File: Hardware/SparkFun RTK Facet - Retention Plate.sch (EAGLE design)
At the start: 31 parts, among them J1 FPC_12_0.5MM2, J16 microSD, J17 NANO_SIM, J2 FPC_12_0.5MM2, U13 LIS2DH12

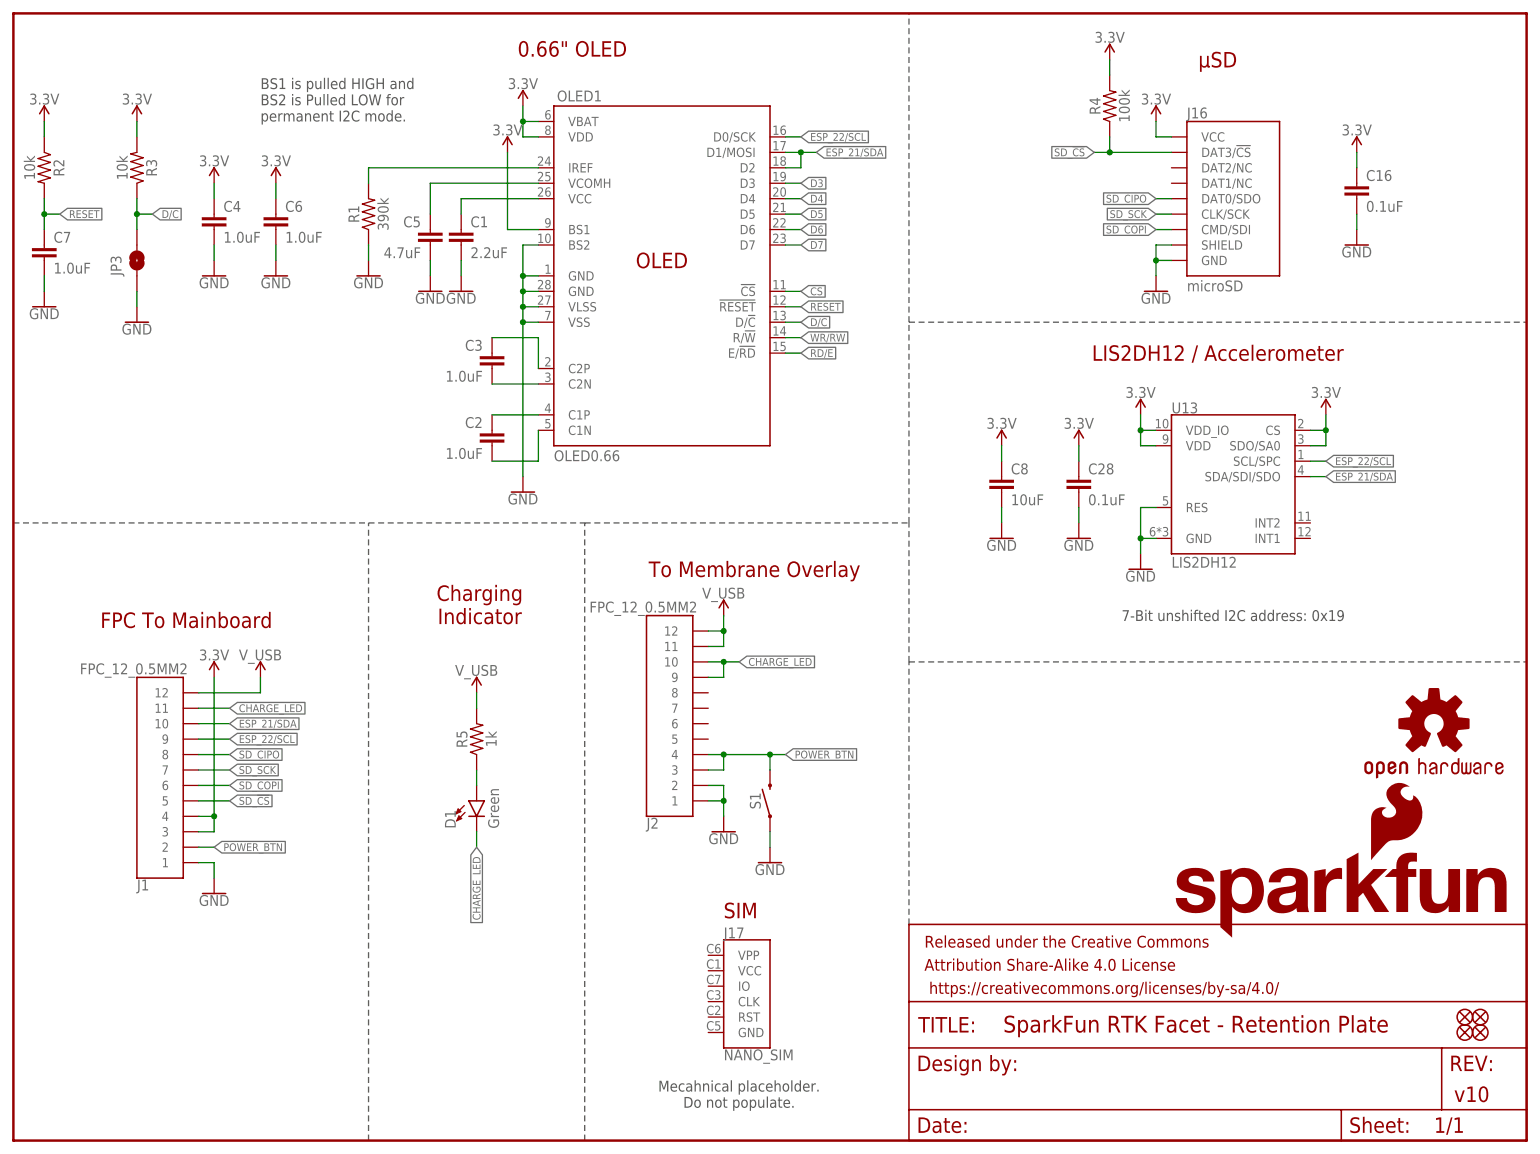
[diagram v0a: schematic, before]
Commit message: Move display connector to side so overlay connector can be center. Notch PCBs. Add dummy PCB height. Add dummy retention plate.
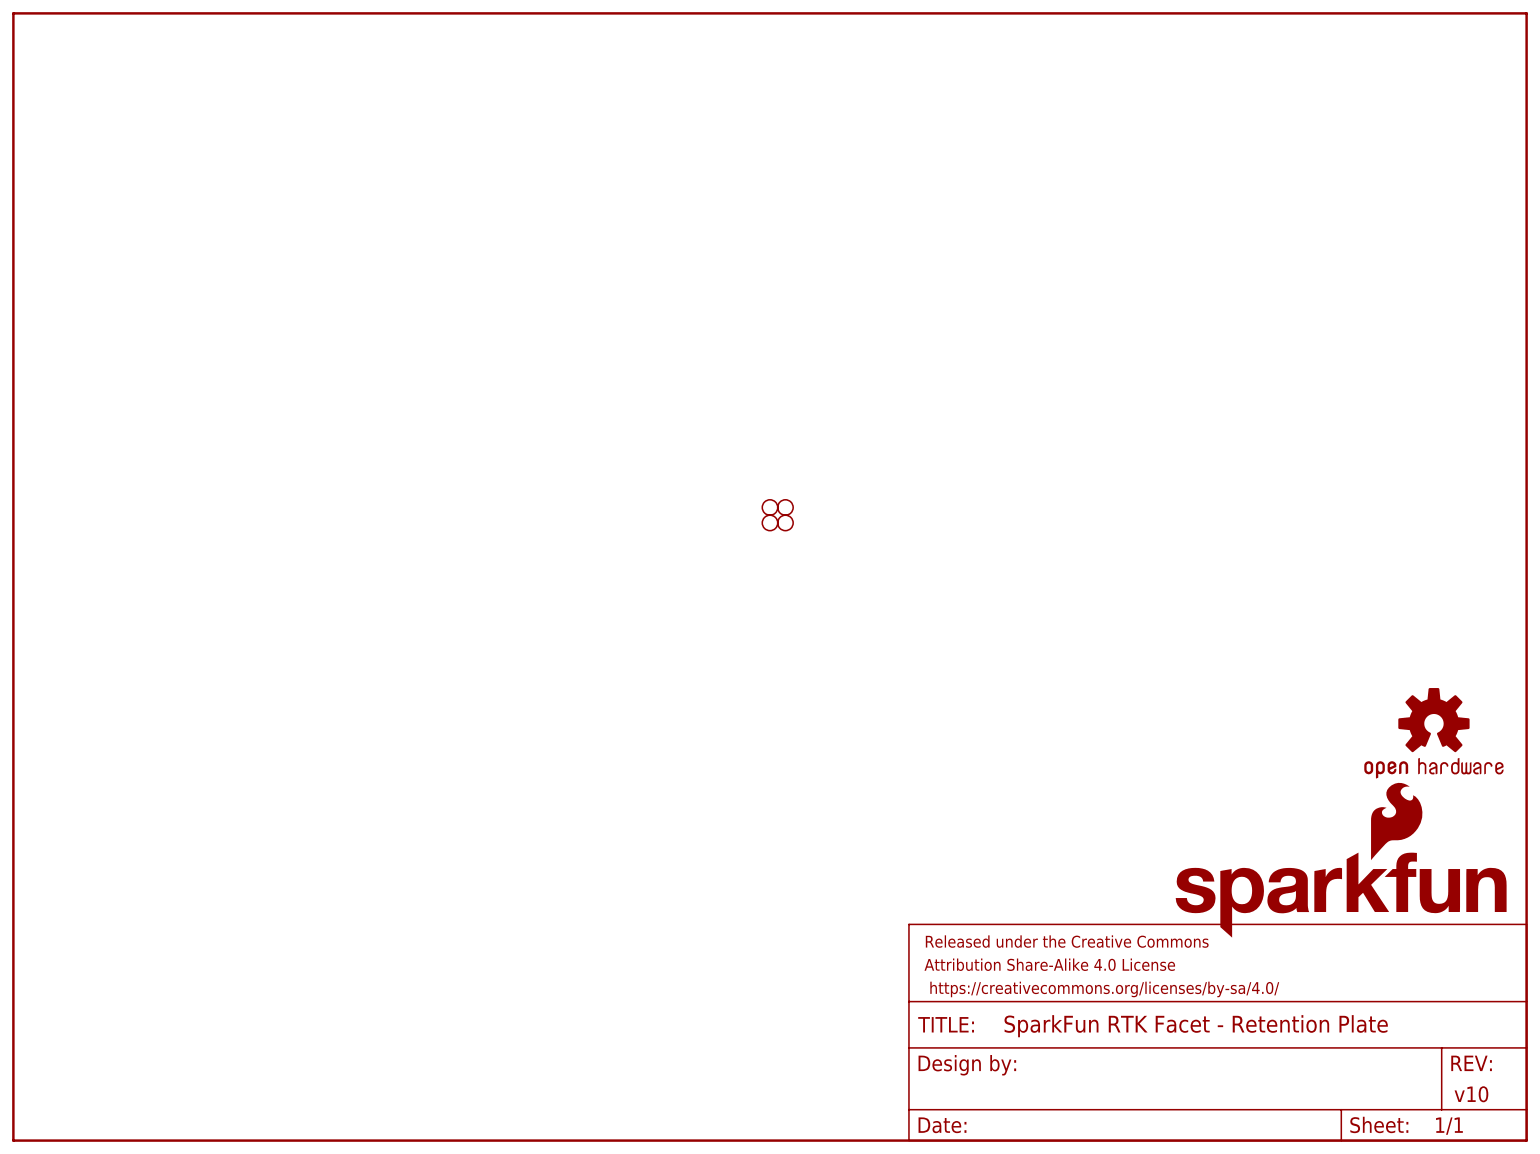
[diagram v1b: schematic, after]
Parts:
- removed C1: 2.2uF, SparkFun-Capacitors:2.2UF-0805-25V-(+80/-20%)
- removed C16, C28: 0.1uF, SparkFun-Capacitors:0.1UF-0603-25V-(+80/-20%)
- removed C2, C3: 1.0uF, SparkFun-Capacitors:1.0UF-0805-25V-10%
- removed C4, C6, C7: 1.0uF, SparkFun-Capacitors:1.0UF-0603-16V-10%
- removed C5: 4.7uF, SparkFun-Capacitors:4.7UF-1206-16V-(+80/-20%)
- removed C8: 10uF, SparkFun-Capacitors:10UF-0603-6.3V-20%
- removed D1: Green, SparkFun-LED:LED-GREEN1206-BOTTOM
- removed FID1, FID2, FID3, FID4: FIDUCIAL1X2, SparkFun-Aesthetics:FIDUCIAL1X2
- removed J1, J2: FPC_12_0.5MM2, RTK Facet:FPC_12_0.5MM2
- removed J16: microSD, SparkFun-Connectors:MICRO-SD-SDIOPUSH-PUSH
- removed J17: NANO_SIM, ublox:NANO_SIMWURTH
- removed JP3: JUMPER-SMT_2_NO_SILK, SparkFun-Jumpers:JUMPER-SMT_2_NO_SILK
- removed OLED1: OLED0.66, SparkFun-Displays:OLED0.66
- removed R1: 390k, SparkFun-Resistors:390KOHM-0603-1/10W-1%
- removed R2, R3: 10k, SparkFun-Resistors:10KOHM-0603-1/10W-1%
- removed R4: 100k, SparkFun-Resistors:100KOHM-0603-1/10W-1%
- removed R5: 1k, SparkFun-Resistors:1KOHM-0603-1/10W-1%
- removed S1: MOMENTARY-SWITCH-SPST-SMD-5.2MM-TALL, SparkFun-Switches:MOMENTARY-SWITCH-SPST-SMD-5.2MM-TALL
- removed U13: LIS2DH12, SparkFun-Sensors:LIS2DH12
- added H1, H2, H3, H4: STAND-OFF, SparkFun-Hardware:STAND-OFF
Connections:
- removed net 3.3V: C16.1, C28.1, C4.1, C6.1, C8.1, J1.3, J1.4, J16.VCC, OLED1.BS1, OLED1.VBAT, OLED1.VDD, R2.1, R3.2, R4.2, U13.CS, U13.SDO/SA0, U13.VDD, U13.VDD_IO
- removed net C1P: C2.1, OLED1.C1P
- removed net C2N: C3.2, OLED1.C2N
- removed net CHARGE_LED: D1.C, J1.11, J2.10, J2.9
- removed net CS: OLED1.!CS!
- removed net D/C: JP3.2, OLED1.D/!C!, R3.1
- removed net D3: OLED1.D3
- removed net D4: OLED1.D4
- removed net D5: OLED1.D5
- removed net D6: OLED1.D6
- removed net D7: OLED1.D7
- removed net ESP_21/SDA: J1.10, OLED1.D1/MOSI, OLED1.D2, U13.SDA/SDI/SDO
- removed net ESP_22/SCL: J1.9, OLED1.D0/SCK, U13.SCL/SPC
- removed net GND: C1.2, C16.2, C28.2, C4.2, C5.2, C6.2, C7.2, C8.2, J1.1, J16.GND, J16.SHIELD, J2.1, J2.2, JP3.1, OLED1.BS2, OLED1.GND@1, OLED1.GND@2, OLED1.VLSS, OLED1.VSS, R1.1, S1.1, U13.GND, U13.RES
- removed net IREF: OLED1.IREF, R1.2
- removed net N$1: C3.1, OLED1.C2P
- removed net N$2: C2.2, OLED1.C1N
- removed net N$3: D1.A, R5.1
- removed net POWER_BTN: J1.2, J2.3, J2.4, S1.2
- removed net RD/E: OLED1.E/!RD!
- removed net RESET: C7.1, OLED1.!RESET!, R2.2
- removed net SD_!CS!: J1.5, J16.DAT3/!CS!, R4.1
- removed net SD_CIPO: J1.8, J16.DAT0/SDO
- removed net SD_COPI: J1.6, J16.CMD/SDI
- removed net SD_SCK: J1.7, J16.CLK/SCK
- removed net VCC: C1.1, OLED1.VCC
- removed net VCOMH: C5.1, OLED1.VCOMH
- removed net V_USB: J1.12, J2.11, J2.12, R5.2
- removed net WR/RW: OLED1.R/!W!
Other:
- note removed: "0.66" OLED"
- note removed: "7-Bit unshifted I2C address: 0x19"
- note removed: "BS1 is pulled HIGH and BS2 is Pulled LOW for permanent I2C mode."
- note removed: "Charging Indicator"
- note removed: "FPC To Mainboard"
- note removed: "LIS2DH12 / Accelerometer"
- note removed: "Mecahnical placeholder. Do not populate."
- note removed: "SIM"
- note removed: "To Membrane Overlay"
- note removed: "μSD"

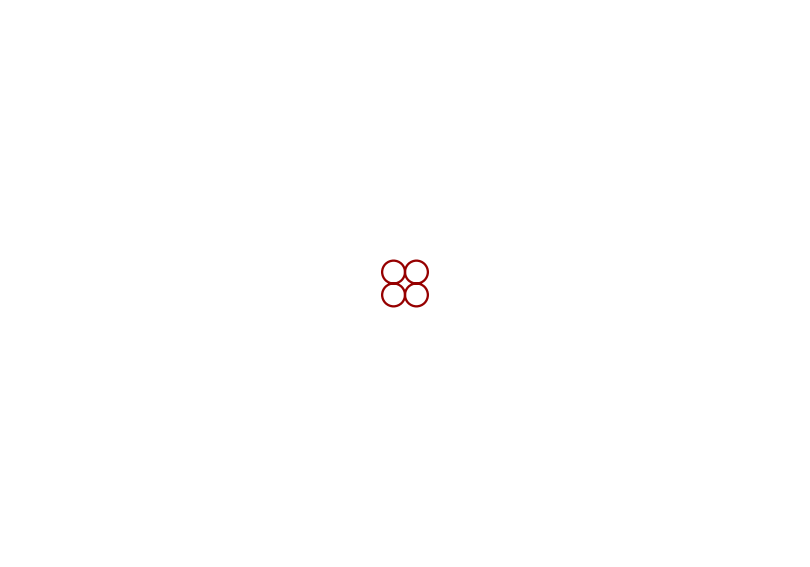
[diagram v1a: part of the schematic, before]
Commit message: Update Retention Plate design as per current Fusion model
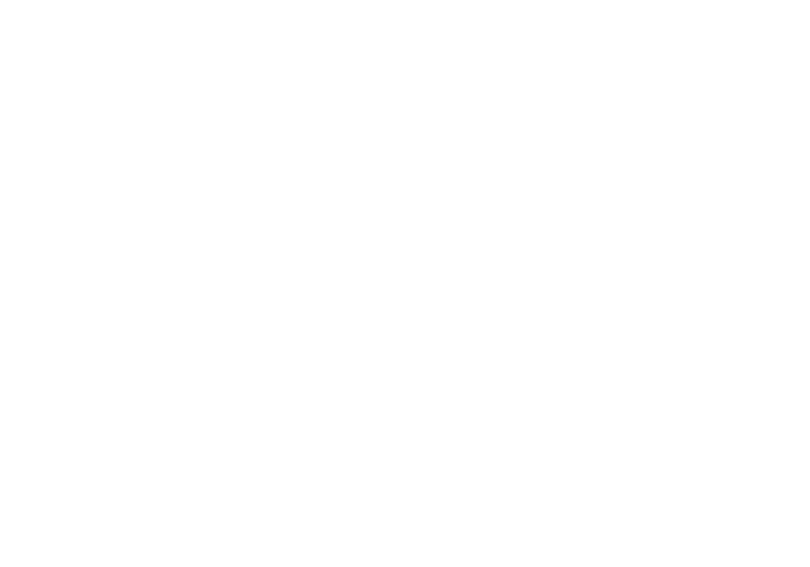
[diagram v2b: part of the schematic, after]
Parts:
- removed H1, H2, H3, H4: STAND-OFF, SparkFun-Hardware:STAND-OFF
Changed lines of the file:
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@@
 <?xml version="1.0" encoding="utf-8"?>
 <!DOCTYPE eagle SYSTEM "eagle.dtd">
-<eagle version="9.6.2">
+<eagle version="9.5.2">
 <drawing>
 <settings>
@@
 <grid distance="0.1" unitdist="inch" unit="inch" style="lines" multiple="1" display="no" altdistance="0.01" altunitdist="inch" altunit="inch"/>
 <layers>
-<layer number="1" name="Top" color="4" fill="1" visible="yes" active="no"/>
-<layer number="2" name="Route2" color="1" fill="3" visible="yes" active="no"/>
-<layer number="3" name="Route3" color="4" fill="3" visible="yes" active="no"/>
-<layer number="4" name="Route4" color="1" fill="4" visible="yes" active="no"/>
-<layer number="5" name="Route5" color="4" fill="4" visible="yes" active="no"/>
-<layer number="6" name="Route6" color="1" fill="8" visible="yes" active="no"/>
-<layer number="7" name="Route7" color="4" fill="8" visible="yes" active="no"/>
-<layer number="8" name="Route8" color="1" fill="2" visible="yes" active="no"/>
-<layer number="9" name="Route9" color="4" fill="2" visible="yes" active="no"/>
-<layer number="10" name="Route10" color="1" fill="7" visible="yes" active="no"/>
-<layer number="11" name="Route11" color="4" fill="7" visible="yes" active="no"/>
-<layer number="12" name="Route12" color="1" fill="5" visible="yes" active="no"/>
-<layer number="13" name="Route13" color="4" fill="5" visible="yes" active="no"/>
-<layer number="14" name="Route14" color="1" fill="6" visible="yes" active="no"/>
-<layer number="15" name="Route15" color="4" fill="6" visible="yes" active="no"/>
-<layer number="16" name="Bottom" color="1" fill="1" visible="yes" active="no"/>
-<layer number="17" name="Pads" color="2" fill="1" visible="yes" active="no"/>
-<layer number="18" name="Vias" color="2" fill="1" visible="yes" active="no"/>
-<layer number="19" name="Unrouted" color="6" fill="1" visible="yes" active="no"/>
-<layer number="20" name="Dimension" color="24" fill="1" visible="yes" active="no"/>
-<layer number="21" name="tPlace" color="16" fill="1" visible="yes" active="no"/>
-<layer number="22" name="bPlace" color="14" fill="1" visible="yes" active="no"/>
-<layer number="23" name="tOrigins" color="15" fill="1" visible="yes" active="no"/>
-<layer number="24" name="bOrigins" color="15" fill="1" visible="yes" active="no"/>
-<layer number="25" name="tNames" color="7" fill="1" visible="yes" active="no"/>
-<layer number="26" name="bNames" color="7" fill="1" visible="yes" active="no"/>
-<layer number="27" name="tValues" color="7" fill="1" visible="yes" active="no"/>
-<layer number="28" name="bValues" color="7" fill="1" visible="yes" active="no"/>
+<layer number="1" name="Top" color="4" fill="1" visible="no" active="no"/>
+<layer number="2" name="Route2" color="1" fill="3" visible="no" active="no"/>
+<layer number="3" name="Route3" color="4" fill="3" visible="no" active="no"/>
+<layer number="4" name="Route4" color="1" fill="4" visible="no" active="no"/>
+<layer number="5" name="Route5" color="4" fill="4" visible="no" active="no"/>
+<layer number="6" name="Route6" color="1" fill="8" visible="no" active="no"/>
+<layer number="7" name="Route7" color="4" fill="8" visible="no" active="no"/>
+<layer number="8" name="Route8" color="1" fill="2" visible="no" active="no"/>
+<layer number="9" name="Route9" color="4" fill="2" visible="no" active="no"/>
+<layer number="10" name="Route10" color="1" fill="7" visible="no" active="no"/>
+<layer number="11" name="Route11" color="4" fill="7" visible="no" active="no"/>
+<layer number="12" name="Route12" color="1" fill="5" visible="no" active="no"/>
+<layer number="13" name="Route13" color="4" fill="5" visible="no" active="no"/>
+<layer number="14" name="Route14" color="1" fill="6" visible="no" active="no"/>
+<layer number="15" name="Route15" color="4" fill="6" visible="no" active="no"/>
+<layer number="16" name="Bottom" color="1" fill="1" visible="no" active="no"/>
+<layer number="17" name="Pads" color="2" fill="1" visible="no" active="no"/>
+<layer number="18" name="Vias" color="2" fill="1" visible="no" active="no"/>
+<layer number="19" name="Unrouted" color="6" fill="1" visible="no" active="no"/>
+<layer number="20" name="Dimension" color="24" fill="1" visible="no" active="no"/>
+<layer number="21" name="tPlace" color="16" fill="1" visible="no" active="no"/>
+<layer number="22" name="bPlace" color="14" fill="1" visible="no" active="no"/>
+<layer number="23" name="tOrigins" color="15" fill="1" visible="no" active="no"/>
+<layer number="24" name="bOrigins" color="15" fill="1" visible="no" active="no"/>
+<layer number="25" name="tNames" color="7" fill="1" visible="no" active="no"/>
+<layer number="26" name="bNames" color="7" fill="1" visible="no" active="no"/>
+<layer number="27" name="tValues" color="7" fill="1" visible="no" active="no"/>
+<layer number="28" name="bValues" color="7" fill="1" visible="no" active="no"/>
 <layer number="29" name="tStop" color="7" fill="3" visible="no" active="no"/>
 <layer number="30" name="bStop" color="7" fill="6" visible="no" active="no"/>
@@
 <layer number="35" name="tGlue" color="7" fill="4" visible="no" active="no"/>
 <layer number="36" name="bGlue" color="7" fill="5" visible="no" active="no"/>
-<layer number="37" name="tTest" color="7" fill="1" visible="yes" active="no"/>
-<layer number="38" name="bTest" color="7" fill="1" visible="yes" active="no"/>
+<layer number="37" name="tTest" color="7" fill="1" visible="no" active="no"/>
+<layer number="38" name="bTest" color="7" fill="1" visible="no" active="no"/>
 <layer number="39" name="tKeepout" color="4" fill="11" visible="no" active="no"/>
 <layer number="40" name="bKeepout" color="1" fill="11" visible="no" active="no"/>
@@
 <layer number="44" name="Drills" color="7" fill="1" visible="no" active="no"/>
 <layer number="45" name="Holes" color="7" fill="1" visible="no" active="no"/>
-<layer number="46" name="Milling" color="3" fill="1" visible="yes" active="no"/>
-<layer number="47" name="Measures" color="7" fill="1" visible="yes" active="no"/>
-<layer number="48" name="Document" color="7" fill="1" visible="yes" active="no"/>
-<layer number="49" name="Reference" color="7" fill="1" visible="yes" active="no"/>
-<layer number="50" name="dxf" color="7" fill="1" visible="yes" active="no"/>
-<layer number="51" name="tDocu" color="6" fill="1" visible="yes" active="no"/>
-<layer number="52" name="bDocu" color="7" fill="1" visible="yes" active="no"/>
-<layer number="53" name="tGND_GNDA" color="7" fill="1" visible="yes" active="no"/>
-<layer number="54" name="bGND_GNDA" color="7" fill="1" visible="yes" active="no"/>
-<layer number="56" name="wert" color="7" fill="1" visible="yes" active="no"/>
-<layer number="57" name="tCAD" color="7" fill="1" visible="yes" active="no"/>
-<layer number="59" name="tCarbon" color="7" fill="1" visible="yes" active="no"/>
-<layer number="60" name="bCarbon" color="7" fill="1" visible="yes" active="no"/>
+<layer number="46" name="Milling" color="3" fill="1" visible="no" active="no"/>
+<layer number="47" name="Measures" color="7" fill="1" visible="no" active="no"/>
+<layer number="48" name="Document" color="7" fill="1" visible="no" active="no"/>
+<layer number="49" name="Reference" color="7" fill="1" visible="no" active="no"/>
+<layer number="50" name="dxf" color="7" fill="1" visible="no" active="no"/>
+<layer number="51" name="tDocu" color="6" fill="1" visible="no" active="no"/>
+<layer number="52" name="bDocu" color="7" fill="1" visible="no" active="no"/>
+<layer number="53" name="tGND_GNDA" color="7" fill="1" visible="no" active="no"/>
+<layer number="54" name="bGND_GNDA" color="7" fill="1" visible="no" active="no"/>
+<layer number="56" name="wert" color="7" fill="1" visible="no" active="no"/>
+<layer number="57" name="tCAD" color="7" fill="1" visible="no" active="no"/>
+<layer number="59" name="tCarbon" color="7" fill="1" visible="no" active="no"/>
+<layer number="60" name="bCarbon" color="7" fill="1" visible="no" active="no"/>
 <layer number="88" name="SimResults" color="9" fill="1" visible="yes" active="yes"/>
 <layer number="89" name="SimProbes" color="9" fill="1" visible="yes" active="yes"/>
@@
 <part name="LOGO3" library="SparkFun-Aesthetics" deviceset="OSHW-LOGO" device="MINI" value="OSHW-LOGOMINI"/>
 <part name="LOGO5" library="SparkFun-Aesthetics" deviceset="SFE_LOGO_NAME_FLAME" device=".1_INCH"/>
-<part name="H1" library="SparkFun-Hardware" deviceset="STAND-OFF" device=""/>
-<part name="H2" library="SparkFun-Hardware" deviceset="STAND-OFF" device=""/>
-<part name="H3" library="SparkFun-Hardware" deviceset="STAND-OFF" device=""/>
-<part name="H4" library="SparkFun-Hardware" deviceset="STAND-OFF" device=""/>
 </parts>
 <sheets>
@@
 <instance part="LOGO3" gate="G$1" x="233.68" y="68.58" smashed="yes"/>
 <instance part="LOGO5" gate="G$1" x="190.5" y="33.02" smashed="yes"/>
-<instance part="H1" gate="G$1" x="127" y="101.6" smashed="yes"/>
-<instance part="H2" gate="G$1" x="127" y="104.14" smashed="yes"/>
-<instance part="H3" gate="G$1" x="124.46" y="104.14" smashed="yes"/>
-<instance part="H4" gate="G$1" x="124.46" y="101.6" smashed="yes"/>
 </instances>
 <busses>
